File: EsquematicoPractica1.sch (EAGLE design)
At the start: 63 parts, among them IC1 GSOT05C-GS08, J1 M50-3500542, Q1 IRF7416PBF, Q2 IRF7416PBF, U1 MKL27Z64VLH4, U13 TLV274QPWRG4Q1, U2 SFH6156-4TSMD-4_VO-L, U3 MC34063ADR, U4 SFH6156-4TSMD-4_VO-L, U5 SFH6156-4TSMD-4_VO-L, U6 SFH6156-4TSMD-4_VO-L, X1 MINI-USB-SCHIELD-32005-201, Y3 32.768KHZ

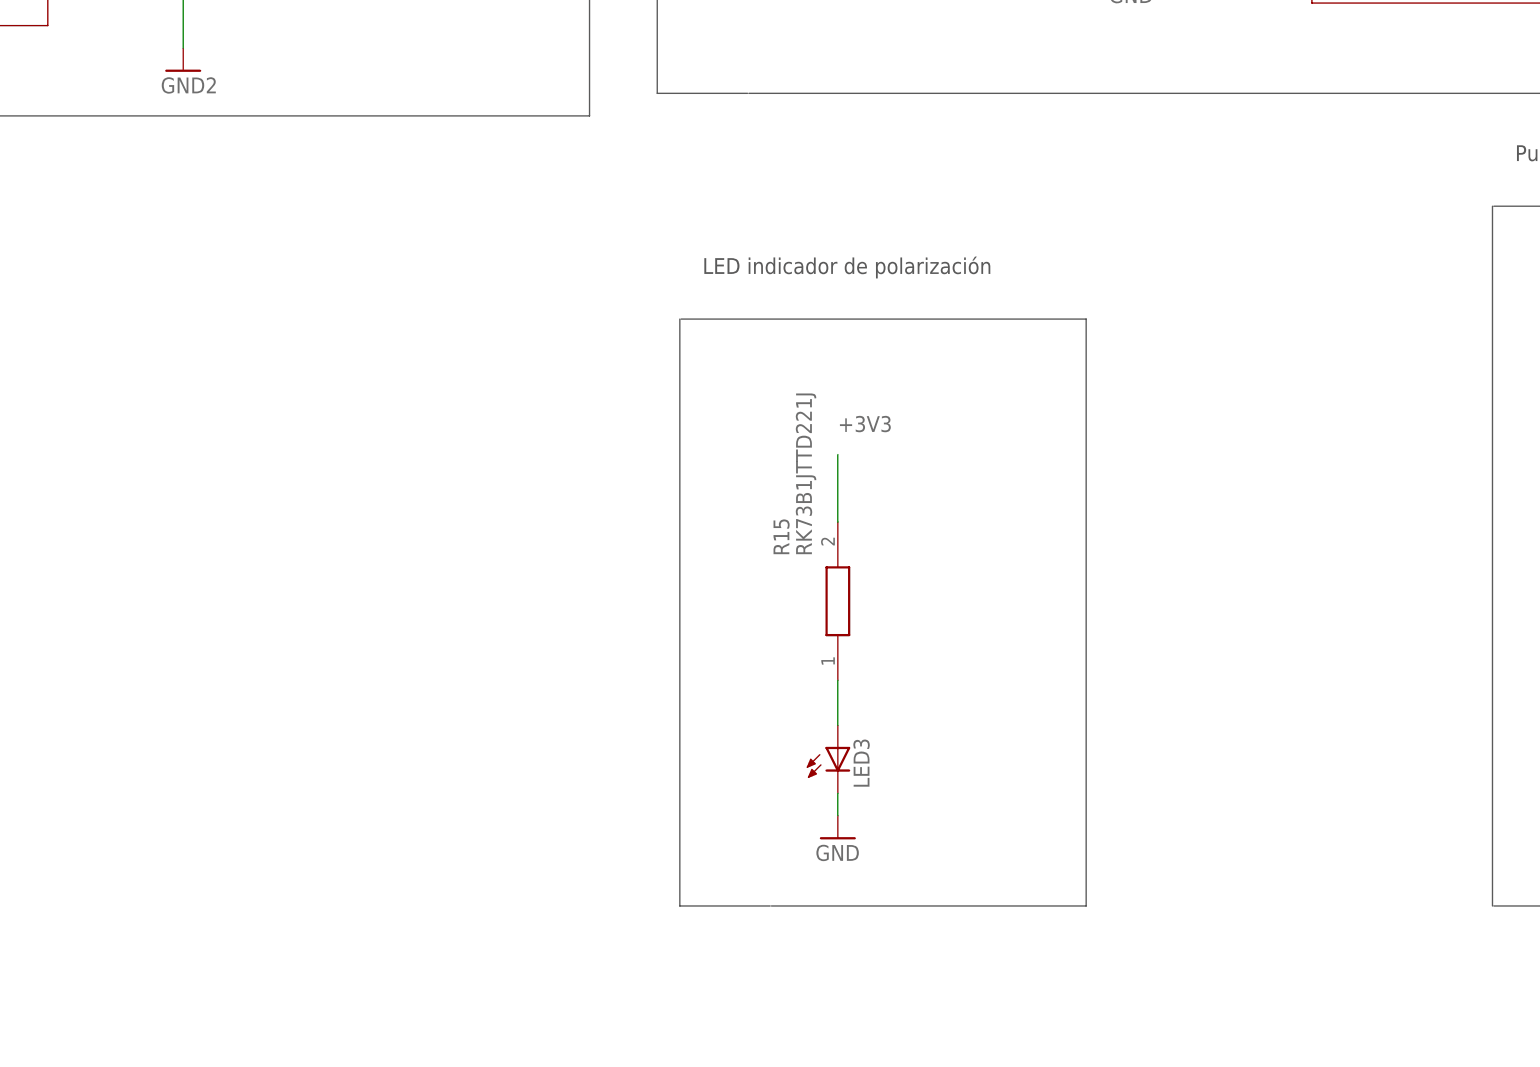
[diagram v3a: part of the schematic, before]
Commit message: con mikroBUS
El esquema del mikroBUS aun no es similar al del profesor pero esta a la medida.
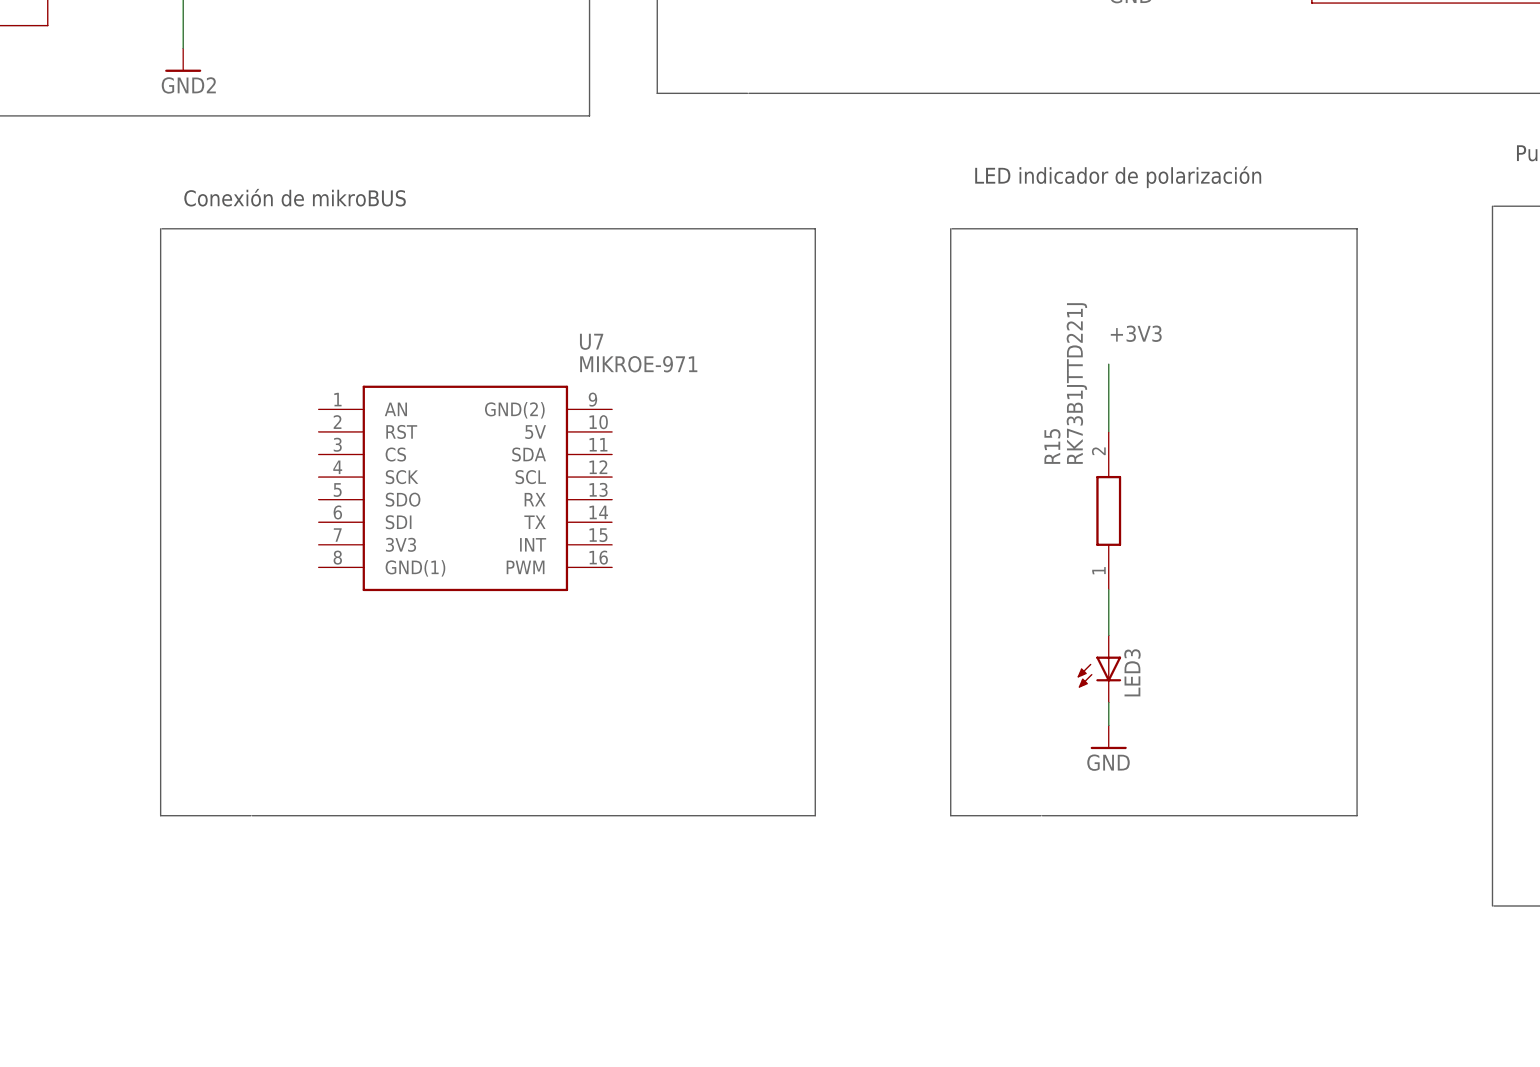
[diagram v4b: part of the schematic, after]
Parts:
- added U7: MIKROE-971, MIKROE-971:MIKROE-971
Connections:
- net +3V3: now also R15.2
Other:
- note added: "Conexión de mikroBUS"
- moved on the sheet: LED3, R15
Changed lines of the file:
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@@
 <part name="R101" library="RC0402FR-0733RL" deviceset="RC0402FR-0733RL" device="" value="33"/>
 <part name="R100" library="RC0402FR-0733RL" deviceset="RC0402FR-0733RL" device="" value="33"/>
+<part name="U7" library="MIKROE-971" deviceset="MIKROE-971" device=""/>
 </parts>
 <sheets>
@@
 <wire x1="-5.08" y1="-78.74" x2="-15.24" y2="-78.74" width="0.1524" layer="97"/>
 <wire x1="-15.24" y1="-78.74" x2="-15.24" y2="-15.24" width="0.1524" layer="97"/>
-<wire x1="33.02" y1="-104.14" x2="-12.5476" y2="-104.14" width="0.1524" layer="97"/>
-<wire x1="33.02" y1="-170.18" x2="33.02" y2="-104.14" width="0.1524" layer="97"/>
-<wire x1="33.02" y1="-170.18" x2="-2.3876" y2="-170.18" width="0.1524" layer="97"/>
-<wire x1="-2.54" y1="-170.18" x2="-12.7" y2="-170.18" width="0.1524" layer="97"/>
-<wire x1="-12.7" y1="-170.18" x2="-12.7" y2="-104.14" width="0.1524" layer="97"/>
-<text x="-10.16" y="-99.06" size="1.778" layer="97">LED indicador de polarización</text>
+<wire x1="63.5" y1="-93.98" x2="17.9324" y2="-93.98" width="0.1524" layer="97"/>
+<wire x1="63.5" y1="-160.02" x2="63.5" y2="-93.98" width="0.1524" layer="97"/>
+<wire x1="63.5" y1="-160.02" x2="28.0924" y2="-160.02" width="0.1524" layer="97"/>
+<wire x1="27.94" y1="-160.02" x2="17.78" y2="-160.02" width="0.1524" layer="97"/>
+<wire x1="17.78" y1="-160.02" x2="17.78" y2="-93.98" width="0.1524" layer="97"/>
+<text x="20.32" y="-88.9" size="1.778" layer="97">LED indicador de polarización</text>
 <wire x1="170.18" y1="-91.44" x2="78.8924" y2="-91.44" width="0.1524" layer="97"/>
 <wire x1="170.18" y1="-170.18" x2="170.18" y2="-91.44" width="0.1524" layer="97"/>
@@
 <text x="490.22" y="60.96" size="1.778" layer="97">32KHz CLK</text>
 <text x="213.36" y="-73.66" size="1.778" layer="97">2 ENTRADAS 0-10 V CON AISLAMIENTO DE IMPEDANCIAS</text>
+<wire x1="2.54" y1="-93.98" x2="-70.9676" y2="-93.98" width="0.1524" layer="97"/>
+<wire x1="2.54" y1="-160.02" x2="2.54" y2="-93.98" width="0.1524" layer="97"/>
+<wire x1="2.54" y1="-160.02" x2="-60.8076" y2="-160.02" width="0.1524" layer="97"/>
+<wire x1="-60.96" y1="-160.02" x2="-71.12" y2="-160.02" width="0.1524" layer="97"/>
+<wire x1="-71.12" y1="-160.02" x2="-71.12" y2="-93.98" width="0.1524" layer="97"/>
+<text x="-68.58" y="-91.44" size="1.778" layer="97">Conexión de mikroBUS</text>
 </plain>
 <instances>
@@
 <instance part="OUT2" gate="-1" x="129.54" y="-55.88" rot="R180"/>
 <instance part="3.3V1" gate="-1" x="114.3" y="-27.94" rot="R270"/>
-<instance part="LED3" gate="G$1" x="5.08" y="-152.4"/>
-<instance part="GND12" gate="1" x="5.08" y="-162.56"/>
+<instance part="LED3" gate="G$1" x="35.56" y="-142.24"/>
+<instance part="GND12" gate="1" x="35.56" y="-152.4"/>
 <instance part="S1" gate="G$1" x="99.06" y="-129.54"/>
 <instance part="GND13" gate="1" x="91.44" y="-147.32"/>
@@
 <instance part="C5" gate="G$1" x="137.16" y="-124.46" rot="R90"/>
 <instance part="C6" gate="G$1" x="137.16" y="-152.4" rot="R90"/>
-<instance part="R15" gate="G$1" x="5.08" y="-144.78" rot="R90"/>
+<instance part="R15" gate="G$1" x="35.56" y="-134.62" rot="R90"/>
 <instance part="X1" gate="G$1" x="220.98" y="2.54" rot="R180"/>
 <instance part="X1" gate="S" x="220.98" y="12.7" rot="R180"/>
@@
 <instance part="R101" gate="G$1" x="276.86" y="2.54"/>
 <instance part="R100" gate="G$1" x="281.94" y="-7.62"/>
+<instance part="U7" gate="G$1" x="-53.34" y="-114.3"/>
 </instances>
 <busses>
@@
 <pinref part="GND12" gate="1" pin="GND"/>
 <pinref part="LED3" gate="G$1" pin="C"/>
-<wire x1="5.08" y1="-160.02" x2="5.08" y2="-157.48" width="0.1524" layer="91"/>
+<wire x1="35.56" y1="-149.86" x2="35.56" y2="-147.32" width="0.1524" layer="91"/>
 </segment>
 <segment>
@@
 <segment>
 <pinref part="LED3" gate="G$1" pin="A"/>
-<wire x1="5.08" y1="-149.86" x2="5.08" y2="-144.78" width="0.1524" layer="91"/>
+<wire x1="35.56" y1="-139.7" x2="35.56" y2="-134.62" width="0.1524" layer="91"/>
 <pinref part="R15" gate="G$1" pin="1"/>
 </segment>
@@
 </segment>
 <segment>
-<wire x1="5.08" y1="-127" x2="5.08" y2="-119.38" width="0.1524" layer="91"/>
-<label x="5.08" y="-116.84" size="1.778" layer="95"/>
-</segment>
-</net>
+<wire x1="35.56" y1="-116.84" x2="35.56" y2="-109.22" width="0.1524" layer="91"/>
+<label x="35.56" y="-106.68" size="1.778" layer="95"/>
+<pinref part="R15" gate="G$1" pin="2"/>
+</segment>
+</net>

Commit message: Con dos entradas de 0-4mA.
Esta completo falta revisar los pines y conectarlos a la KL.
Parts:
- removed U7: MIKROE-971, MIKROE-971:MIKROE-971
- added C10, C17, C18, C7: 10u, rcl:C-USC0805
- added C11, C13, C19, C21: 1u, rcl:C-USC0805
- added C12, C14, C16, C20, C22, C9: 0.1u, rcl:C-USC0805
- added C15, C8: 0.33u, rcl:C-USC0805
- added IC2, IC5: RCV420JP, RCV420JP:RCV420JP
- added IC3, IC6: TC7662BEOA, TC7662BEOA:TC7662BEOA
- added IC4, IC7: MC7812BTG, MC7812BTG:MC7812BTG
- added IN_CORRIENTE_4-1, IN_CORRIENTE_4-20: (no value), pinhead:PINHD-1X1
- added R14, R16, R18, R19: 10K, rcl:R-US_M0805
- added R17, R20: 10k, rcl:R-US_M0805
- added U$1: MIKROE_CLICKMINI, mikrobus_lib:MIKROE_CLICKMINI
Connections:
- new net N$27: C7.1, IC3.CAP+
- new net N$29: C11.1, C12.1, C9.1, IC2.V+, IC3.V+, IC4.OUT
- new net N$30: C7.2, IC3.CAP-
- new net N$31: IC2.REF_FB, IC2.REF_OUT
- new net N$32: R14.1, R16.2
- new net N$33: C10.1, C13.1, C14.1, IC2.V-, IC3.VOUT
- new net N$34: R16.1, R17.2
- new net N$35: IC2.RCV_FB, IC2.RCV_OUT, R14.2
- new net N$36: IC2.-IN, IN_CORRIENTE_4-20.1
- new net N$37: C16.1, C19.1, C20.1, IC5.V+, IC6.V+, IC7.OUT
- new net N$38: C17.1, IC6.CAP+
- new net N$39: C17.2, IC6.CAP-
- new net N$40: C18.1, C21.1, C22.1, IC5.V-, IC6.VOUT
- new net N$41: IC5.REF_FB, IC5.REF_OUT
- new net N$42: IC5.RCV_FB, IC5.RCV_OUT, R18.2
- new net N$43: R18.1, R19.2
- new net N$44: R19.1, R20.2
- new net N$45: IC5.-IN, IN_CORRIENTE_4-1.1
- net GND: now also C10.2, C11.2, C12.2, C13.2, C14.2, C15.2, C16.2, C18.2, C19.2, C20.2, C21.2, C22.2, C8.2, C9.2, IC2.CT, IC2.RCV_COM, IC2.REF_COM, IC2.REF_IN, IC3.GND, IC3.LOW_VOLTAGE_LV, IC4.GND, IC5.CT, IC5.RCV_COM, IC5.REF_COM, IC5.REF_IN, IC6.GND, IC6.LOW_VOLTAGE_LV, IC7.GND, R17.1, R20.1
- net VCC: now also C15.1, C8.1, IC4.IN, IC7.IN
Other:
- note added: "Entradas (0-20)mA"
